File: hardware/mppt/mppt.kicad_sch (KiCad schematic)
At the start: 0 parts

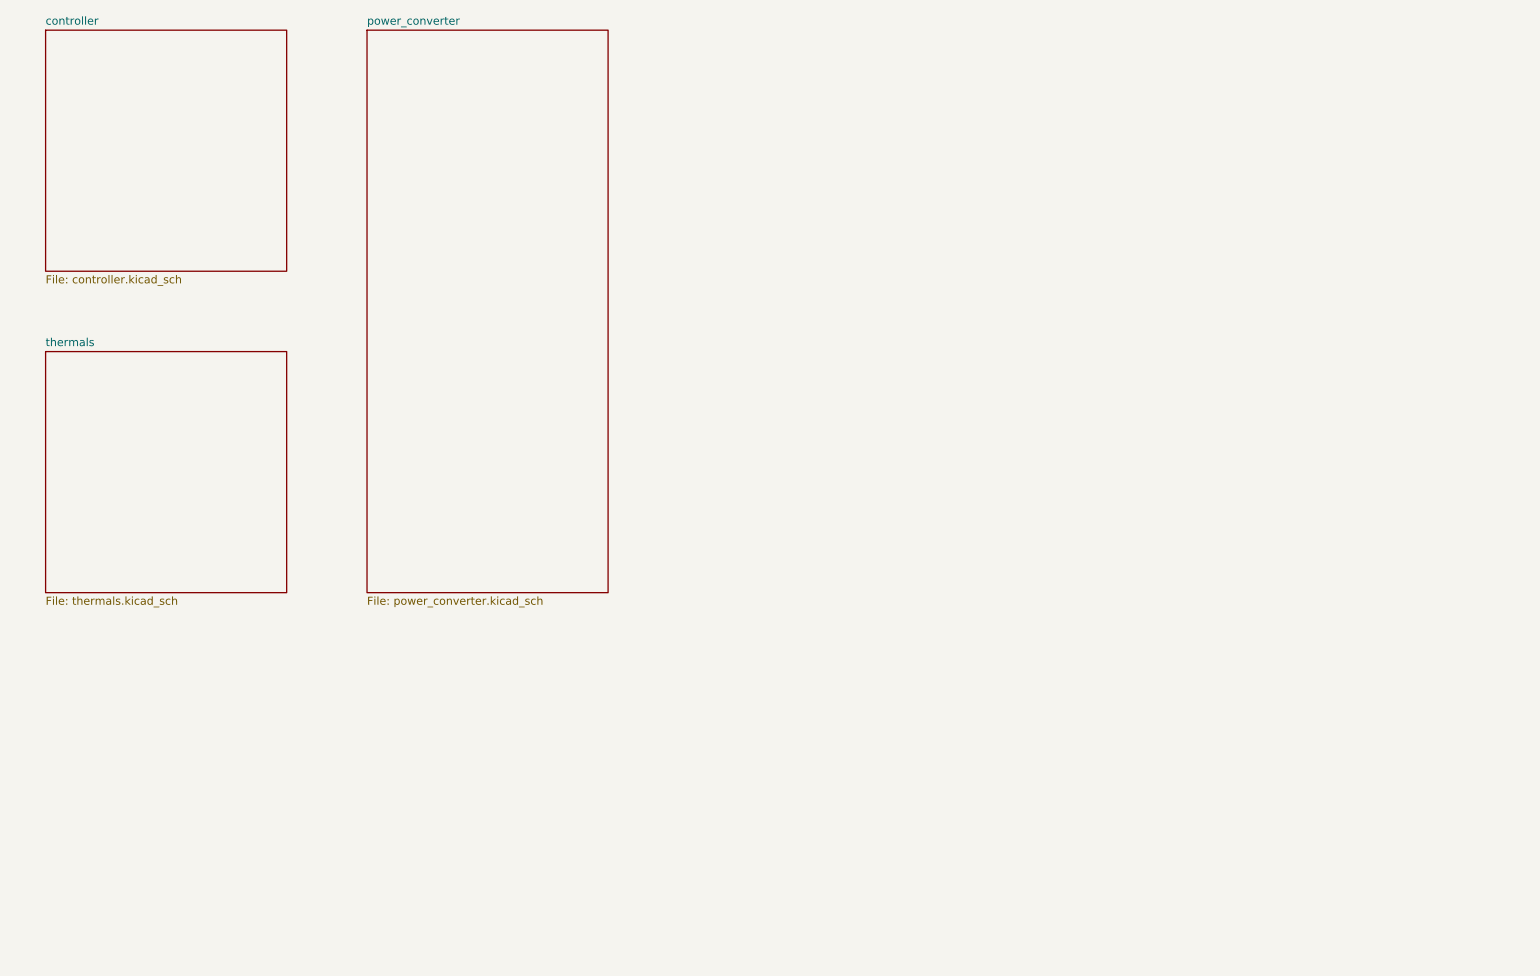
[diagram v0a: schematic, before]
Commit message: run through mppt sch, going through bom
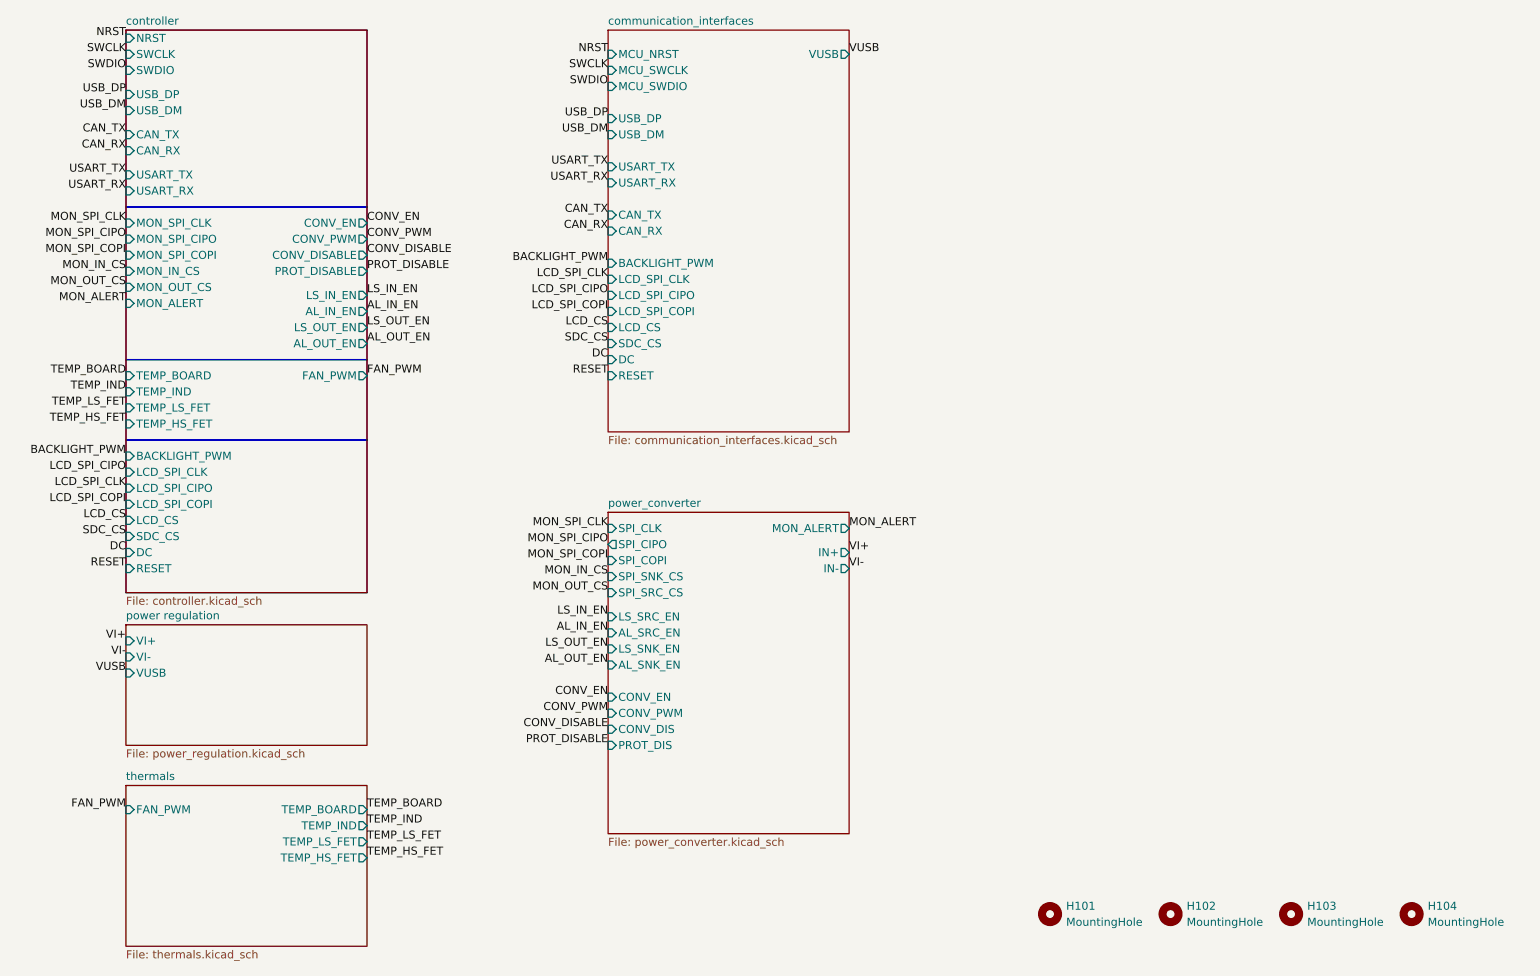
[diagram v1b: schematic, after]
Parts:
- added H101, H102, H103, H104: MountingHole, MountingHole:MountingHole_5.3mm_M5, symbol Mechanical:MountingHole
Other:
- added sheet communication_interfaces (communication_interfaces.kicad_sch)
- added sheet power regulation (power_regulation.kicad_sch)
- sheet controller ports: added AL_IN_EN, AL_OUT_EN, BACKLIGHT_PWM, CAN_RX, CAN_TX, CONV_DISABLE, CONV_EN, CONV_PWM, DC, FAN_PWM, LCD_CS, LCD_SPI_CIPO, LCD_SPI_CLK, LCD_SPI_COPI, LS_IN_EN, LS_OUT_EN, MON_ALERT, MON_IN_CS, MON_OUT_CS, MON_SPI_CIPO, MON_SPI_CLK, MON_SPI_COPI, NRST, PROT_DISABLE, RESET, SDC_CS, SWCLK, SWDIO, TEMP_BOARD, TEMP_HS_FET, TEMP_IND, TEMP_LS_FET, USART_RX, USART_TX, USB_DM, USB_DP; removed none
- sheet power_converter ports: added AL_SNK_EN, AL_SRC_EN, CONV_DIS, CONV_EN, CONV_PWM, IN+, IN-, LS_SNK_EN, LS_SRC_EN, MON_ALERT, PROT_DIS, SPI_CIPO, SPI_CLK, SPI_COPI, SPI_SNK_CS, SPI_SRC_CS; removed none
- sheet thermals ports: added FAN_PWM, TEMP_BOARD, TEMP_HS_FET, TEMP_IND, TEMP_LS_FET; removed none

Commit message: bom consolidated, starting layout
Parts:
- H101, H102, H103, H104: footprint MountingHole:MountingHole_5.3mm_M5 -> MountingHole:MountingHole_3.2mm_M3; Notes M5 Hole -> M3 Hole
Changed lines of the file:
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@@
 			)
 		)
-		(property "Footprint" "MountingHole:MountingHole_5.3mm_M5"
-			(at 222.25 165.1 0)
-			(effects
-				(font
-					(size 1.27 1.27)
-				)
-				(hide yes)
-			)
-		)
-		(property "Datasheet" ""
-			(at 222.25 165.1 0)
-			(effects
-				(font
-					(size 1.27 1.27)
-				)
-				(hide yes)
-			)
-		)
-		(property "Description" "Mounting Hole without connection"
-			(at 222.25 165.1 0)
-			(effects
-				(font
-					(size 1.27 1.27)
-				)
-				(hide yes)
-			)
-		)
-		(property "Notes" "M5 Hole"
-			(at 222.25 165.1 0)
-			(effects
-				(font
-					(size 1.27 1.27)
-				)
-				(hide yes)
-			)
-		)
-		(property "Sim.Device" ""
-			(at 222.25 165.1 0)
-			(effects
-				(font
-					(size 1.27 1.27)
-				)
-				(hide yes)
-			)
-		)
-		(property "Sim.Pins" ""
+		(property "Footprint" "MountingHole:MountingHole_3.2mm_M3"
+			(at 222.25 165.1 0)
+			(effects
+				(font
+					(size 1.27 1.27)
+				)
+				(hide yes)
+			)
+		)
+		(property "Datasheet" ""
+			(at 222.25 165.1 0)
+			(effects
+				(font
+					(size 1.27 1.27)
+				)
+				(hide yes)
+			)
+		)
+		(property "Description" "Mounting Hole without connection"
+			(at 222.25 165.1 0)
+			(effects
+				(font
+					(size 1.27 1.27)
+				)
+				(hide yes)
+			)
+		)
+		(property "Notes" "M3 Hole"
 			(at 222.25 165.1 0)
 			(effects
@@
 			)
 		)
-		(property "Footprint" "MountingHole:MountingHole_5.3mm_M5"
-			(at 184.15 165.1 0)
-			(effects
-				(font
-					(size 1.27 1.27)
-				)
-				(hide yes)
-			)
-		)
-		(property "Datasheet" ""
-			(at 184.15 165.1 0)
-			(effects
-				(font
-					(size 1.27 1.27)
-				)
-				(hide yes)
-			)
-		)
-		(property "Description" "Mounting Hole without connection"
-			(at 184.15 165.1 0)
-			(effects
-				(font
-					(size 1.27 1.27)
-				)
-				(hide yes)
-			)
-		)
-		(property "Notes" "M5 Hole"
-			(at 184.15 165.1 0)
-			(effects
-				(font
-					(size 1.27 1.27)
-				)
-				(hide yes)
-			)
-		)
-		(property "Sim.Device" ""
-			(at 184.15 165.1 0)
-			(effects
-				(font
-					(size 1.27 1.27)
-				)
-				(hide yes)
-			)
-		)
-		(property "Sim.Pins" ""
+		(property "Footprint" "MountingHole:MountingHole_3.2mm_M3"
+			(at 184.15 165.1 0)
+			(effects
+				(font
+					(size 1.27 1.27)
+				)
+				(hide yes)
+			)
+		)
+		(property "Datasheet" ""
+			(at 184.15 165.1 0)
+			(effects
+				(font
+					(size 1.27 1.27)
+				)
+				(hide yes)
+			)
+		)
+		(property "Description" "Mounting Hole without connection"
+			(at 184.15 165.1 0)
+			(effects
+				(font
+					(size 1.27 1.27)
+				)
+				(hide yes)
+			)
+		)
+		(property "Notes" "M3 Hole"
 			(at 184.15 165.1 0)
 			(effects
@@
 			)
 		)
-		(property "Footprint" "MountingHole:MountingHole_5.3mm_M5"
-			(at 241.3 165.1 0)
-			(effects
-				(font
-					(size 1.27 1.27)
-				)
-				(hide yes)
-			)
-		)
-		(property "Datasheet" ""
-			(at 241.3 165.1 0)
-			(effects
-				(font
-					(size 1.27 1.27)
-				)
-				(hide yes)
-			)
-		)
-		(property "Description" "Mounting Hole without connection"
-			(at 241.3 165.1 0)
-			(effects
-				(font
-					(size 1.27 1.27)
-				)
-				(hide yes)
-			)
-		)
-		(property "Notes" "M5 Hole"
-			(at 241.3 165.1 0)
-			(effects
-				(font
-					(size 1.27 1.27)
-				)
-				(hide yes)
-			)
-		)
-		(property "Sim.Device" ""
-			(at 241.3 165.1 0)
-			(effects
-				(font
-					(size 1.27 1.27)
-				)
-				(hide yes)
-			)
-		)
-		(property "Sim.Pins" ""
+		(property "Footprint" "MountingHole:MountingHole_3.2mm_M3"
+			(at 241.3 165.1 0)
+			(effects
+				(font
+					(size 1.27 1.27)
+				)
+				(hide yes)
+			)
+		)
+		(property "Datasheet" ""
+			(at 241.3 165.1 0)
+			(effects
+				(font
+					(size 1.27 1.27)
+				)
+				(hide yes)
+			)
+		)
+		(property "Description" "Mounting Hole without connection"
+			(at 241.3 165.1 0)
+			(effects
+				(font
+					(size 1.27 1.27)
+				)
+				(hide yes)
+			)
+		)
+		(property "Notes" "M3 Hole"
 			(at 241.3 165.1 0)
 			(effects
@@
 			)
 		)
-		(property "Footprint" "MountingHole:MountingHole_5.3mm_M5"
-			(at 203.2 165.1 0)
-			(effects
-				(font
-					(size 1.27 1.27)
-				)
-				(hide yes)
-			)
-		)
-		(property "Datasheet" ""
-			(at 203.2 165.1 0)
-			(effects
-				(font
-					(size 1.27 1.27)
-				)
-				(hide yes)
-			)
-		)
-		(property "Description" "Mounting Hole without connection"
-			(at 203.2 165.1 0)
-			(effects
-				(font
-					(size 1.27 1.27)
-				)
-				(hide yes)
-			)
-		)
-		(property "Notes" "M5 Hole"
-			(at 203.2 165.1 0)
-			(effects
-				(font
-					(size 1.27 1.27)
-				)
-				(hide yes)
-			)
-		)
-		(property "Sim.Device" ""
-			(at 203.2 165.1 0)
-			(effects
-				(font
-					(size 1.27 1.27)
-				)
-				(hide yes)
-			)
-		)
-		(property "Sim.Pins" ""
-			(at 203.2 165.1 0)
-			(effects
+		(property "Footprint" "MountingHole:MountingHole_3.2mm_M3"
+			(at 203.2 165.1 0)
+			(effects
+				(font
+					(size 1.27 1.27)
+				)
+				(hide yes)
+			)
+		)
+		(property "Datasheet" ""
+			(at 203.2 165.1 0)
+			(effects
+				(font
+					(size 1.27 1.27)
+				)
+				(hide yes)
+			)
+		)
+		(property "Description" "Mounting Hole without connection"
+			(at 203.2 165.1 0)
+			(effects
+				(font
+					(size 1.27 1.27)
+				)
+				(hide yes)
+			)
+		)
+		(property "Notes" "M3 Hole"
+			(at 203.2 165.1 0)
+			(effects

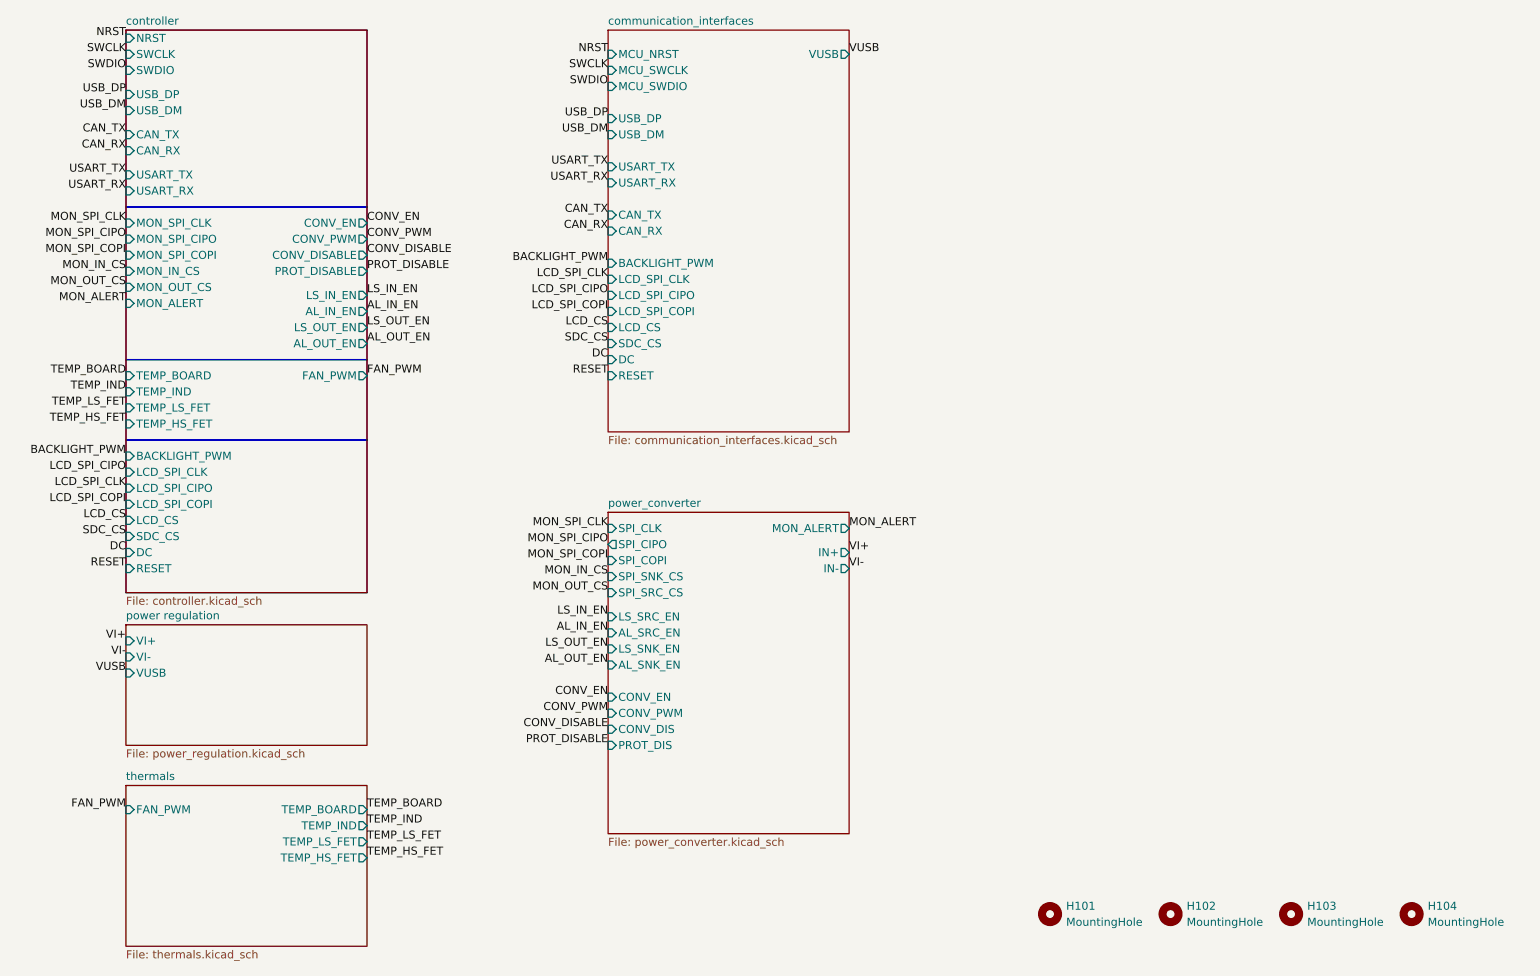
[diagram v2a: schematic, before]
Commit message: PCB variant for power regulation breakout.
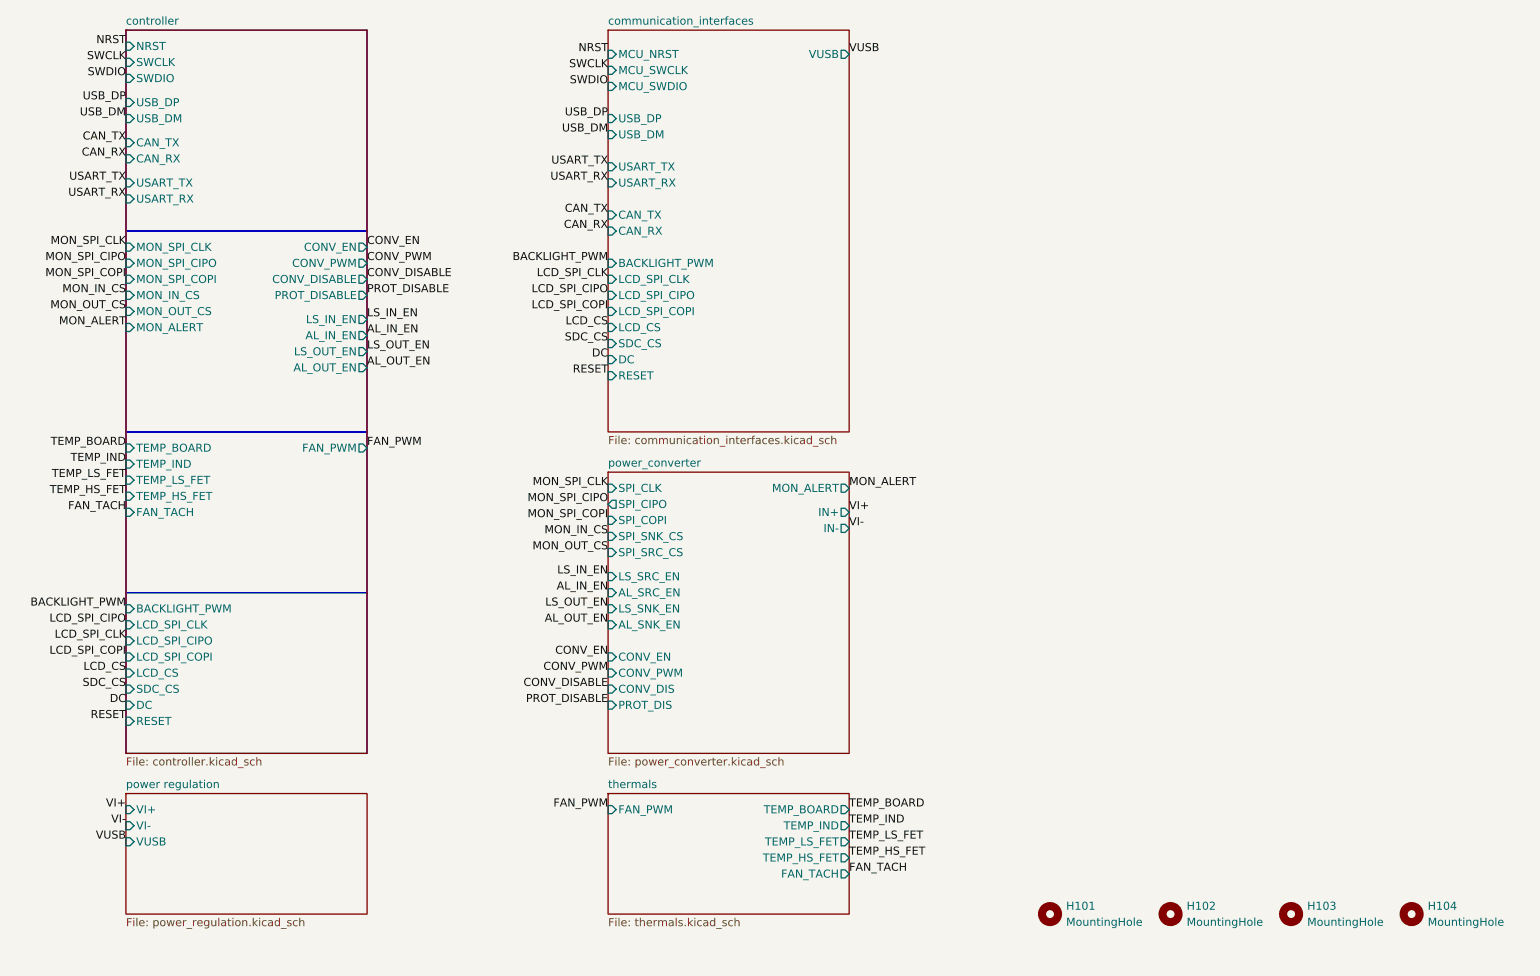
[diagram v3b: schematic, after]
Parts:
- H101, H102, H103, H104: footprint MountingHole:MountingHole_3.2mm_M3 -> MountingHole:MountingHole_2.7mm_M2.5_DIN965_Pad_TopBottom; Notes M3 Hole -> M2.5 Hole
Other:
- sheet controller ports: added FAN_TACH; removed none
- sheet thermals ports: added FAN_TACH; removed none
